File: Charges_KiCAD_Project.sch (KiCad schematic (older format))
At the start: 17 parts

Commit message: Updated PCB
Finalized most of the charges board and PCB
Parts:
- removed C?: 860160272005 5v 47micro farad, Capacitor_THT:C_Radial_D5.0mm_H11.0mm_P2.00mm, symbol SparkFun-Capacitors:10UF-POLAR-0603-6.3V-20%_TANT_
- removed C?: 100nF, symbol Device:C_Small
- removed J?: ARM 10 Pin, 2X5-RA, symbol SparkFun-Connectors:CONN_05X2RA
- removed J?: CONN_06X2SMD_FEMALE, 2X6_SMD, symbol SparkFun-Connectors:CONN_06X2SMD_FEMALE
- removed Q? (x2): MOSFET-NCH-2N7002PW, SOT323, symbol SparkFun-DiscreteSemi:MOSFET-NCH-2N7002PW
- added C1, C2, C3, C4: CP1_Small, Capacitor_THT:CP_Axial_L10.0mm_D4.5mm_P15.00mm_Horizontal, symbol Device:CP1_Small
- added J2: Screw_Terminal_01x04, TerminalBlock_Phoenix:TerminalBlock_Phoenix_PTSM-0,5-4-2.5-V-THR_1x04_P2.50mm_Vertical, symbol Connector:Screw_Terminal_01x04
- added Q1, Q2: SI7232DN-T1-GE3, SamacSys_Parts:SI7232DNT1GE3, symbol SamacSys_Parts:SI7232DN-T1-GE3
- added R11, R13: 10k, Resistor_SMD:R_0603_1608Metric, symbol SparkFun-Resistors:RESISTOR0402
- added R15, R19: 100k, Resistor_SMD:R_0603_1608Metric, symbol SparkFun-Resistors:RESISTOR0402
- added R16, R17, R4, R5: 10, Resistor_SMD:R_0603_1608Metric, symbol SparkFun-Resistors:RESISTOR0402
- added R20, R21, R8, R9: 0.25, Resistor_SMD:R_0603_1608Metric, symbol SparkFun-Resistors:RESISTOR0402
- added R23, R25: 27k, Resistor_SMD:R_0603_1608Metric, symbol SparkFun-Resistors:RESISTOR0402
- added R3, R7: 1k, Resistor_SMD:R_0603_1608Metric, symbol SparkFun-Resistors:RESISTOR0402
- BZ1: renamed from BZ?; footprint (none) -> Buzzer_Beeper:Buzzer_12x9.5RM7.6
- J1: renamed from J?; footprint (none) -> TerminalBlock_Phoenix:TerminalBlock_Phoenix_PTSM-0,5-4-2.5-V-THR_1x04_P2.50mm_Vertical
- R1: renamed from R?; footprint (none) -> Resistor_SMD:R_0603_1608Metric
- R10, R12, R14, R2, R22, R24: renamed from R?; footprint 0402 -> Resistor_SMD:R_0603_1608Metric
- R18, R6: renamed from R?; value 3.3k -> 10k; footprint 0402 -> Resistor_SMD:R_0603_1608Metric
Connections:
- net labels added: Alert_Active, Alert_scl, Alert_sda, Fet_C, Fet_D, Fire, Fire_C, Fire_D, Fire_Redundant, NRST, SWCLK, SWDIO, Sense_C, Sense_D
- net labels removed: I2C1_SCL, I2C1_SDA
- wire segments 46 -> 113
- no-connect marks 11 -> 3
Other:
- note removed: "Current version uses connector data\nbus for communications to BMS.\nThis may not be ideal, and perhaps a \ndedicated communcation line\nto the BMS should be used instead."
- note removed: "Main System Bus"
- note removed: "NRST cap protects\nagainst parasitic resets."
- note removed: "SWD Connector"
- moved on the sheet: BZ1, J1, R1, R10, R12, R14, R18, R2, R22, R24, R6

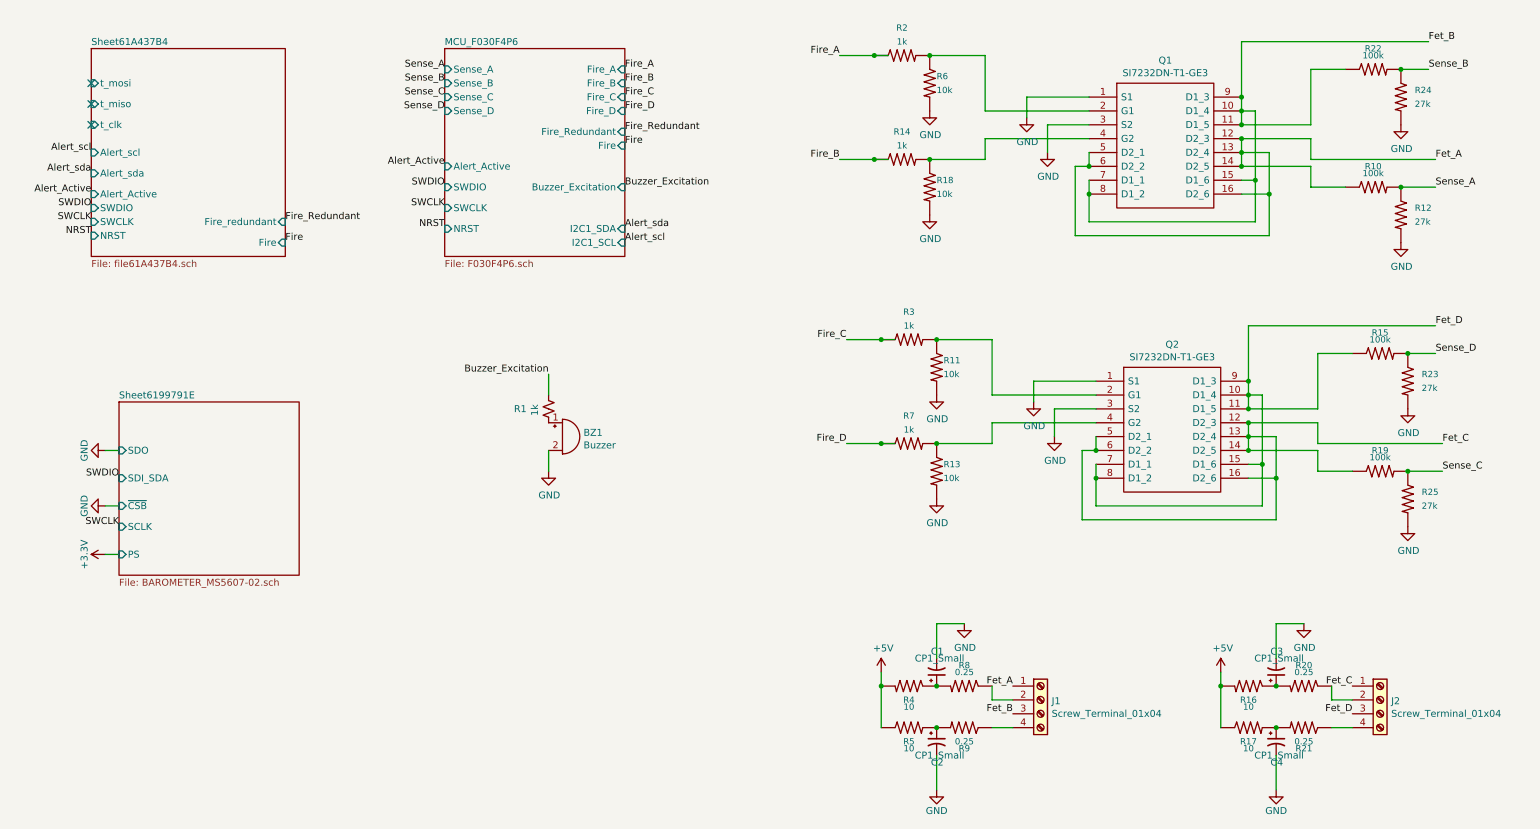
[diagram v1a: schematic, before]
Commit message: Fix to components
Changed the buzzer and terminal blocks
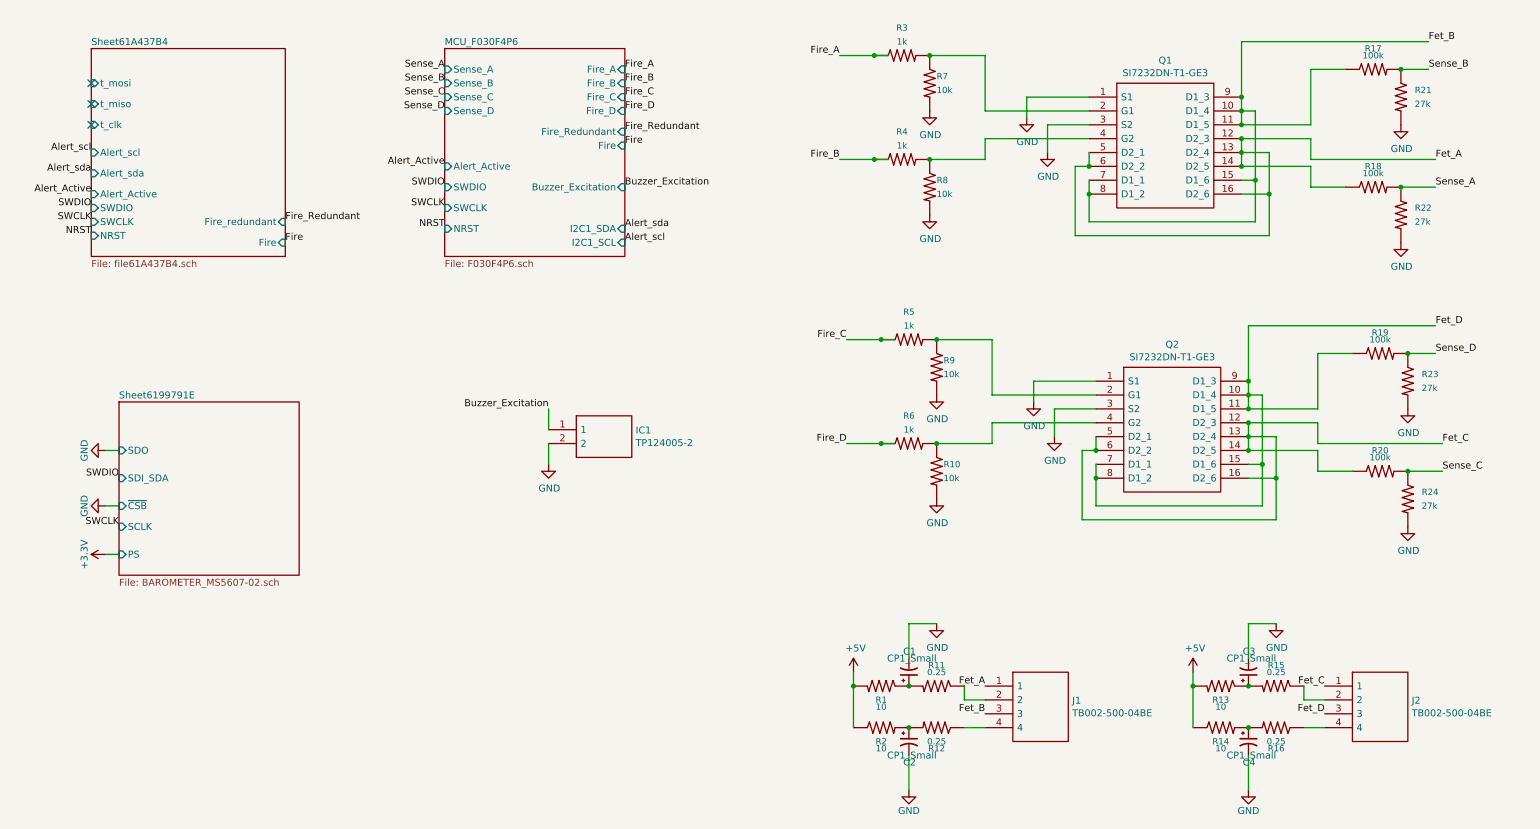
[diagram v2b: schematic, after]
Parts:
- removed BZ1: Buzzer, Buzzer_Beeper:Buzzer_12x9.5RM7.6, symbol Device:Buzzer
- removed J1, J2: Screw_Terminal_01x04, TerminalBlock_Phoenix:TerminalBlock_Phoenix_PTSM-0,5-4-2.5-V-THR_1x04_P2.50mm_Vertical, symbol Connector:Screw_Terminal_01x04
- removed R1: 1k, Resistor_SMD:R_0603_1608Metric, symbol Device:R_Small_US
- added IC1: TP124005-2, SamacSys_Parts:TP1240052, symbol SamacSys_Parts:TP124005-2
- added J1, J2: TB002-500-04BE, SamacSys_Parts:TB00250004BE, symbol SamacSys_Parts:TB002-500-04BE
- renumbered R4 to R1, R13 to R10, R8 to R11, R9 to R12, R16 to R13, R17 to R14, R20 to R15, R21 to R16, R22 to R17, R10 to R18, R15 to R19, R5 to R2, R19 to R20, R24 to R21, R12 to R22, R25 to R24, R2 to R3, R14 to R4, R3 to R5, R7 to R6, R6 to R7, R18 to R8, R11 to R9
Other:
- moved on the sheet: C1, C2, C3, C4, R1, R11, R12, R13, R14, R15, R16, R2

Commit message: updated pcb
pcb updated to the right size
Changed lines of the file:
@@
 	0    1    1    0
 $EndComp
-Text Label 10700 3750 0    50   ~ 0
+Text Label 10650 2900 0    50   ~ 0
 Fet_C
 $Comp
@@
 Wire Wire Line
 	10450 3950 10700 3950
-Text Label 10700 3950 0    50   ~ 0
+Text Label 10650 3100 0    50   ~ 0
 Sense_C
 Text Label 6400 3750 2    50   ~ 0
@@
 Text Label 6400 3000 2    50   ~ 0
 Fire_C
-Text Label 10650 3100 0    50   ~ 0
+Text Label 10700 3950 0    50   ~ 0
 Sense_D
 Connection ~ 10450 3100
 Wire Wire Line
 	10450 3100 10650 3100
-Text Label 10650 2900 0    50   ~ 0
+Text Label 10700 3750 0    50   ~ 0
 Fet_D
 $Comp
@@
 Wire Wire Line
 	8150 1850 8150 1950
-$Comp
-L SamacSys_Parts:SI7232DN-T1-GE3 Q1
-U 1 1 61A5982E
-P 8150 1250
-F 0 "Q1" H 8700 1515 50  0000 C CNN
-F 1 "SI7232DN-T1-GE3" H 8700 1424 50  0000 C CNN
-F 2 "SamacSys_Parts:SI7232DNT1GE3" H 9100 1350 50  0001 L CNN
-F 3 "https://www.vishay.com/docs/68986/si7232dn.pdf" H 9100 1250 50  0001 L CNN
-F 4 "Dual N-Channel (D-S)MOSFET 20V Vds 8V Vgs PowerPAK 1212-8 " H 9100 1150 50  0001 L CNN "Description"
-F 5 "1.12" H 9100 1050 50  0001 L CNN "Height"
-F 6 "781-SI7232DN-GE3" H 9100 950 50  0001 L CNN "Mouser Part Number"
-F 7 "https://www.mouser.co.uk/ProductDetail/Vishay-Semiconductors/SI7232DN-T1-GE3?qs=%252BPu8jn5UVnH5FJ8Jo4EbFw%3D%3D" H 9100 850 50  0001 L CNN "Mouser Price/Stock"
-F 8 "Vishay" H 9100 750 50  0001 L CNN "Manufacturer_Name"
-F 9 "SI7232DN-T1-GE3" H 9100 650 50  0001 L CNN "Manufacturer_Part_Number"
-	1    8150 1250
-	1    0    0    -1
-$EndComp
 $Comp
 L power:+5V #PWR016
@@
 Wire Wire Line
 	9850 5800 9700 5800
-Text Label 10650 1700 0    50   ~ 0
+Text Label 10600 850  0    50   ~ 0
 Fet_A
 Text Label 3500 1150 2    50   ~ 0
@@
 $EndComp
 Wire Wire Line
-	6700 1700 6600 1700
-Wire Wire Line
 	10400 1900 10650 1900
-Text Label 10650 1900 0    50   ~ 0
+Text Label 10600 1050 0    50   ~ 0
 Sense_A
 Text Label 6350 1700 2    50   ~ 0
@@
 Text Label 6350 950  2    50   ~ 0
 Fire_A
-Text Label 10600 1050 0    50   ~ 0
+Text Label 10650 1900 0    50   ~ 0
 Sense_B
 Connection ~ 10400 1050
 Wire Wire Line
 	10400 1050 10600 1050
-Text Label 10600 850  0    50   ~ 0
+Text Label 10650 1700 0    50   ~ 0
 Fet_B
 $Comp
@@
 	1    10400 2100
 	0    1    1    0
-$EndComp
-$Comp
-L SparkFun-Resistors:RESISTOR0402 R18
-U 1 1 617B3C91
-P 10200 1900
-F 0 "R18" H 10200 2050 45  0000 C CNN
-F 1 "100k" H 10200 2000 45  0000 C CNN
-F 2 "Resistor_SMD:R_0603_1608Metric" H 10200 2050 20  0001 C CNN
-F 3 "" H 10200 1900 60  0001 C CNN
-F 4 " " H 10200 2021 60  0000 C CNN "Field4"
-	1    10200 1900
-	1    0    0    -1
 $EndComp
 $Comp
@@
 	1    0    0    -1
 $EndComp
+$Comp
+L SparkFun-Resistors:RESISTOR0402 R18
+U 1 1 617B3C91
+P 10200 1900
+F 0 "R18" H 10200 2050 45  0000 C CNN
+F 1 "100k" H 10200 2000 45  0000 C CNN
+F 2 "Resistor_SMD:R_0603_1608Metric" H 10200 2050 20  0001 C CNN
+F 3 "" H 10200 1900 60  0001 C CNN
+F 4 " " H 10200 2021 60  0000 C CNN "Field4"
+	1    10200 1900
+	1    0    0    -1
+$EndComp
+Wire Wire Line
+	6700 1700 6600 1700
+$Comp
+L SamacSys_Parts:SI7232DN-T1-GE3 Q1
+U 1 1 61A5982E
+P 8150 1250
+F 0 "Q1" H 8700 1515 50  0000 C CNN
+F 1 "SI7232DN-T1-GE3" H 8700 1424 50  0000 C CNN
+F 2 "SamacSys_Parts:SI7232DNT1GE3" H 9100 1350 50  0001 L CNN
+F 3 "https://www.vishay.com/docs/68986/si7232dn.pdf" H 9100 1250 50  0001 L CNN
+F 4 "Dual N-Channel (D-S)MOSFET 20V Vds 8V Vgs PowerPAK 1212-8 " H 9100 1150 50  0001 L CNN "Description"
+F 5 "1.12" H 9100 1050 50  0001 L CNN "Height"
+F 6 "781-SI7232DN-GE3" H 9100 950 50  0001 L CNN "Mouser Part Number"
+F 7 "https://www.mouser.co.uk/ProductDetail/Vishay-Semiconductors/SI7232DN-T1-GE3?qs=%252BPu8jn5UVnH5FJ8Jo4EbFw%3D%3D" H 9100 850 50  0001 L CNN "Mouser Price/Stock"
+F 8 "Vishay" H 9100 750 50  0001 L CNN "Manufacturer_Name"
+F 9 "SI7232DN-T1-GE3" H 9100 650 50  0001 L CNN "Manufacturer_Part_Number"
+	1    8150 1250
+	1    0    0    -1
+$EndComp
